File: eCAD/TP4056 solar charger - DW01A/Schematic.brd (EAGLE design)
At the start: 71.1 x 28.9 mm, 33 parts, among them IC1 TP4056X, IC2 AP9101CK6-ADTRG1, IC3 FDS6898A, Q1 SI2347DS-T1-GE3, X1 PV_PANEL, X2 BATTERY, X3 OUTPUT

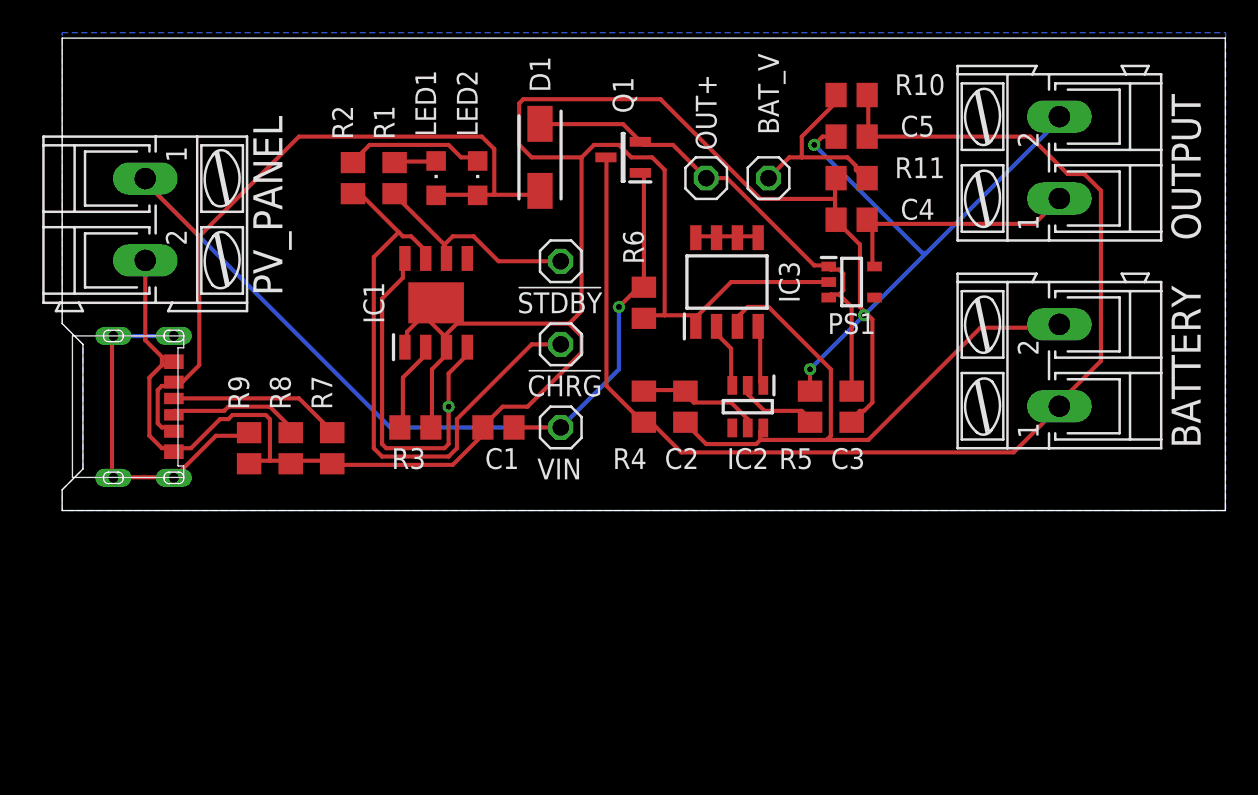
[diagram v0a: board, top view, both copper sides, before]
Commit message: RTC example and test
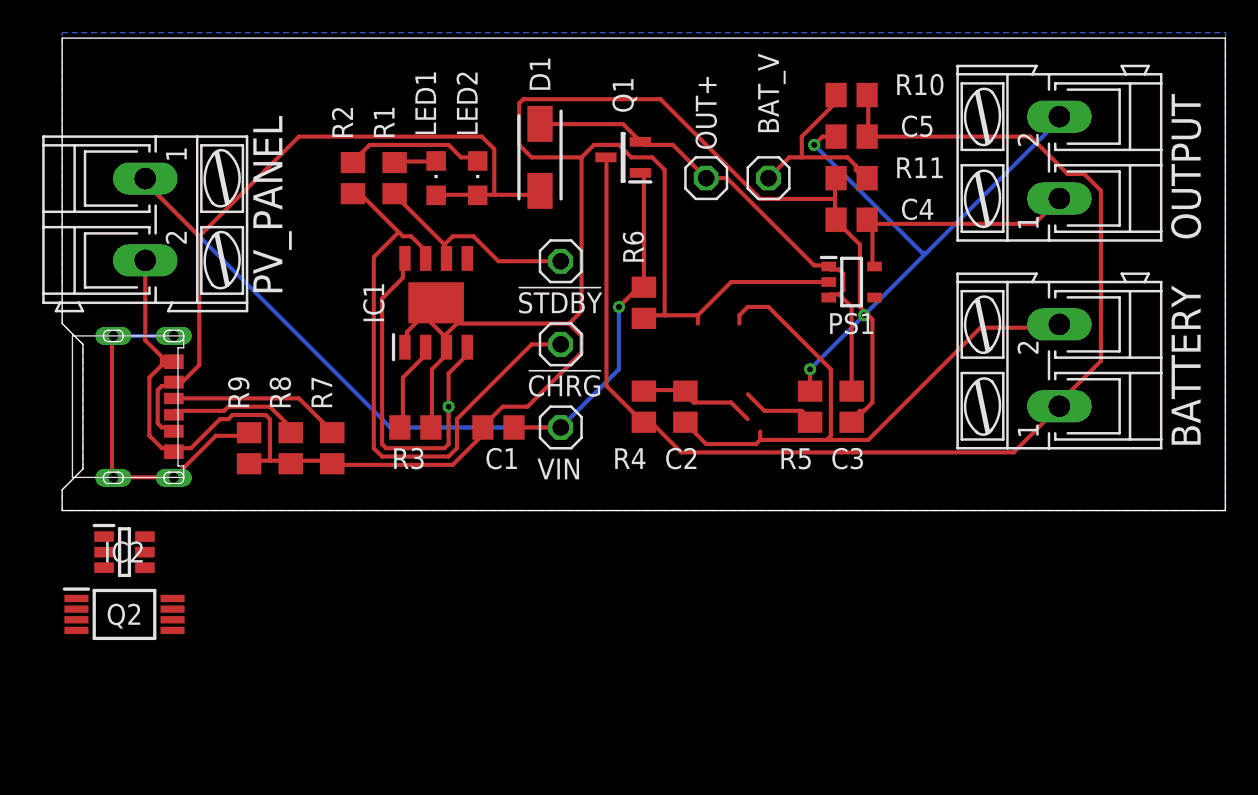
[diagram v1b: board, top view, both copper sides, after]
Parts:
- removed IC3: FDS6898A, 1-component-search:SOIC127P600X175-8N
- added Q2: FS8205A, 1-component-search:SOP65P640X120-8N
- IC2: value AP9101CK6-ADTRG1 -> DW01A-G; device 1-component-search:SOT95P285X140-6N -> 1-component-search:SOT95P280X135-6N
- moved IC2 39.1 mm to (3.81, -2.54), turned to 0 degrees
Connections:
- removed net N$10: IC2.1, IC3.4
- removed net N$12: IC2.3, IC3.2
- removed net N$13: IC3.5, IC3.6, IC3.7, IC3.8
- net BAT-: no longer IC2.6, IC3.3
- net GND: no longer IC3.1
- net N$5: no longer IC2.5
- net N$9: no longer IC2.2
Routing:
- net N$12: track 4.00 -> 0.00 mm
- net N$13: track 3.96 -> 0.00 mm
- net N$10: track 3.75 -> 0.00 mm
- net GND: track 188.8 -> 187.9 mm
- net N$9: track 5.17 -> 4.63 mm
- net N$5: track 7.84 -> 7.30 mm
- net BAT-: track 39.9 -> 39.4 mm

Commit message: DW01A schematic, removed eagle.epf from gitignore
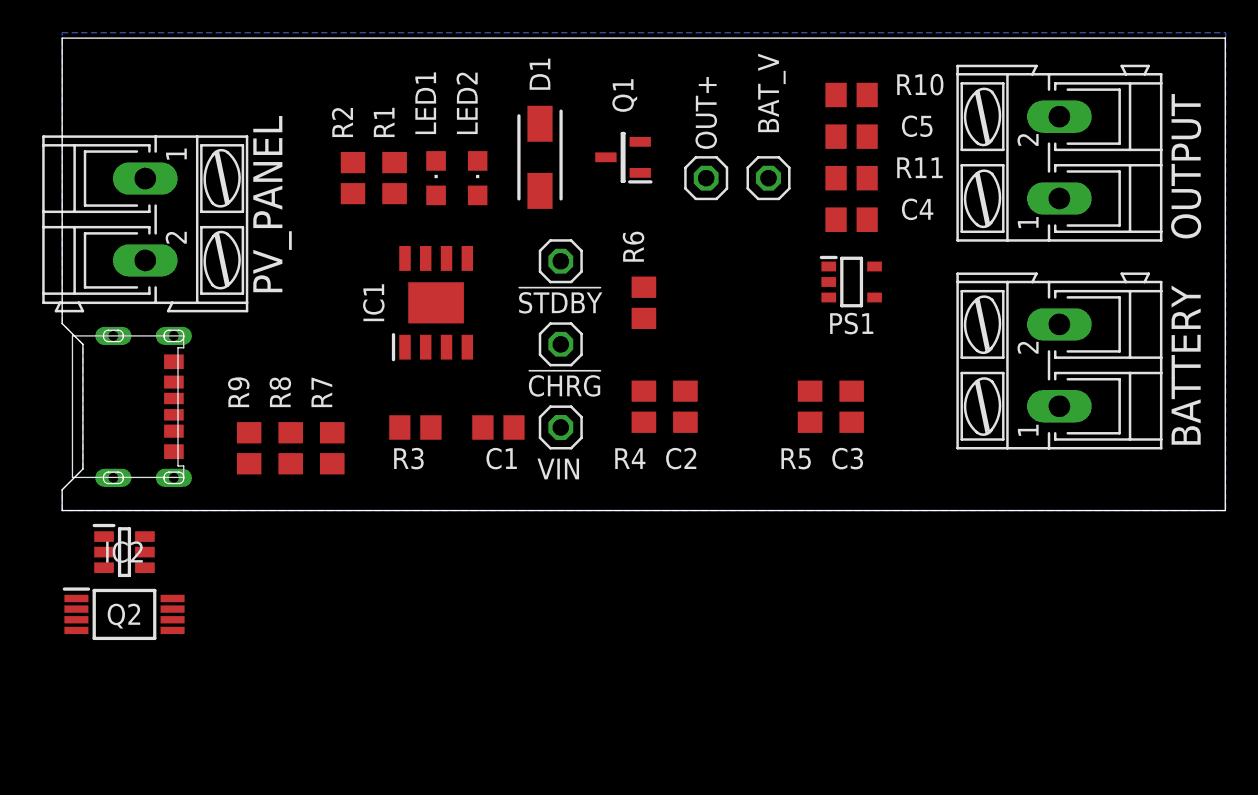
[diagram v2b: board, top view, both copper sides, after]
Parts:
- R4: value 330R -> 100R
- R5: value 2k7 -> 1k
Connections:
- new net N$10: IC2.1, Q2.4
- new net N$12: IC2.3, Q2.5
- net BAT-: now also Q2.2, Q2.3
- net GND: now also IC2.6, Q2.6, Q2.7
- net N$5: now also IC2.5
- net N$9: now also IC2.2
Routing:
- net GND: track 187.9 -> 0.00 mm, vias 3 -> 0
- net VIN: track 126.2 -> 0.00 mm, vias 2 -> 0
- net OUTPUT: track 77.1 -> 0.00 mm
- net BAT-: track 39.4 -> 0.00 mm
- net N$6: track 35.8 -> 0.00 mm
- net OUT+: track 30.7 -> 0.00 mm
- net N$7: track 22.1 -> 0.00 mm
- net N$14: track 15.6 -> 0.00 mm
- net N$3: track 13.2 -> 0.00 mm
- net N$15: track 11.9 -> 0.00 mm
- net N$11: track 10.6 -> 0.00 mm
- net N$2: track 8.64 -> 0.00 mm
- net N$8: track 8.31 -> 0.00 mm
- net N$5: track 7.30 -> 0.00 mm
- net N$4: track 5.69 -> 0.00 mm
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
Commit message: Created version of charger with JLC stock parts
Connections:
- net BAT-: now also IC2.6
- net GND: no longer IC2.6
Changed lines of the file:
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@@
 <contactref element="Q2" pad="6"/>
 <contactref element="Q2" pad="7"/>
-<contactref element="IC2" pad="6"/>
 <wire x1="47.31" y1="22.86" x2="60.96" y2="24.0792" width="0" layer="19" extent="1-1"/>
 <wire x1="47.31" y1="20.32" x2="47.31" y2="22.86" width="0" layer="19" extent="1-1"/>
@@
 <wire x1="6.83" y1="3.6" x2="11.43" y2="2.86" width="0" layer="19" extent="1-1"/>
 <wire x1="6.83" y1="9.1" x2="6.83" y2="3.6" width="0" layer="19" extent="1-1"/>
-<wire x1="5.06" y1="-1.59" x2="6.83" y2="3.6" width="0" layer="19" extent="1-1"/>
-<wire x1="6.748" y1="-6.025" x2="5.06" y2="-1.59" width="0" layer="19" extent="1-1"/>
+<wire x1="5.08" y1="15.2908" x2="6.83" y2="9.1" width="0" layer="19" extent="1-1"/>
+<wire x1="6.748" y1="-6.025" x2="6.83" y2="3.6" width="0" layer="19" extent="1-1"/>
 <wire x1="6.748" y1="-6.675" x2="6.748" y2="-6.025" width="0" layer="19" extent="1-1"/>
-<wire x1="5.08" y1="15.2908" x2="6.83" y2="9.1" width="0" layer="19" extent="1-1"/>
 </signal>
 <signal name="N$5">
@@
 <contactref element="Q2" pad="2"/>
 <contactref element="Q2" pad="3"/>
+<contactref element="IC2" pad="6"/>
 <wire x1="38.1" y1="5.4" x2="60.96" y2="11.3792" width="0" layer="19" extent="1-1"/>
-<wire x1="0.872" y1="-6.025" x2="38.1" y2="5.4" width="0" layer="19" extent="1-1"/>
+<wire x1="5.06" y1="-1.59" x2="38.1" y2="5.4" width="0" layer="19" extent="1-1"/>
+<wire x1="0.872" y1="-6.025" x2="5.06" y2="-1.59" width="0" layer="19" extent="1-1"/>
 <wire x1="0.872" y1="-6.675" x2="0.872" y2="-6.025" width="0" layer="19" extent="1-1"/>
 </signal>

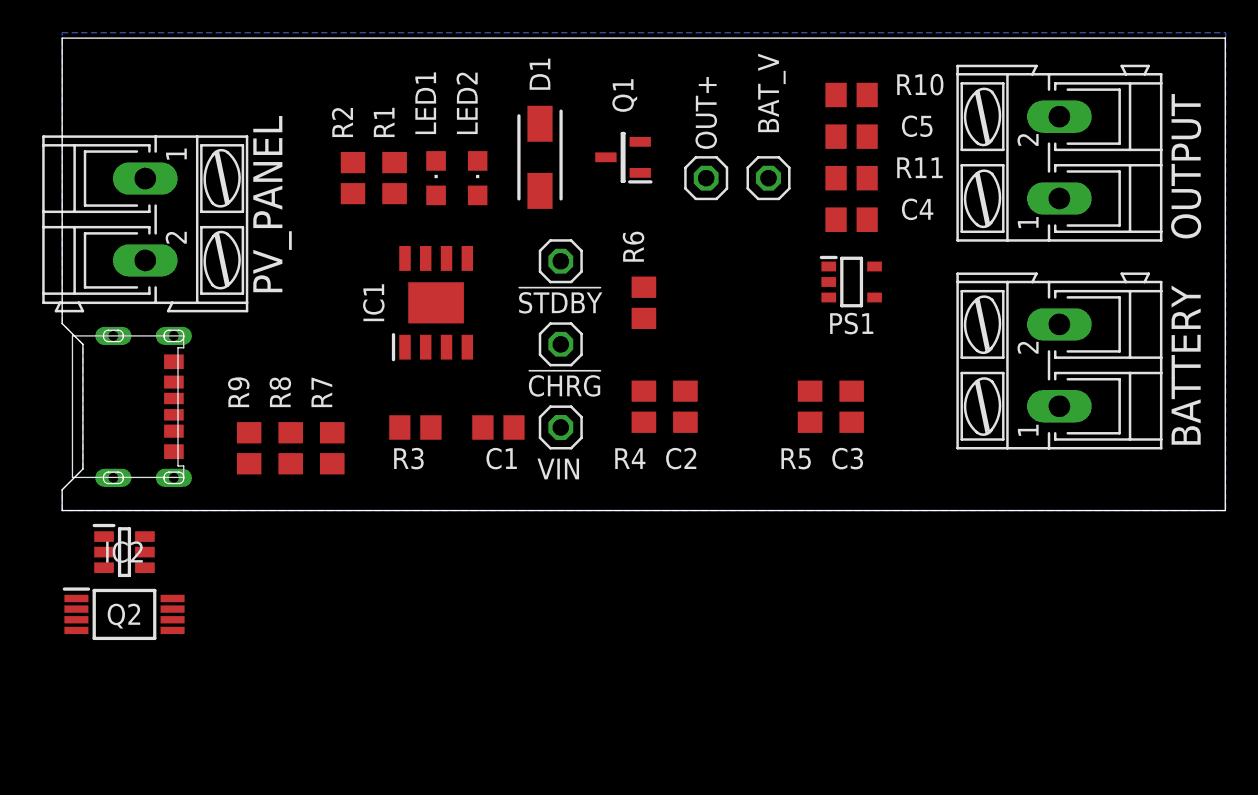
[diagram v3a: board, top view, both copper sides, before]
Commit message: Added power circuits, connection to Quectel devkit
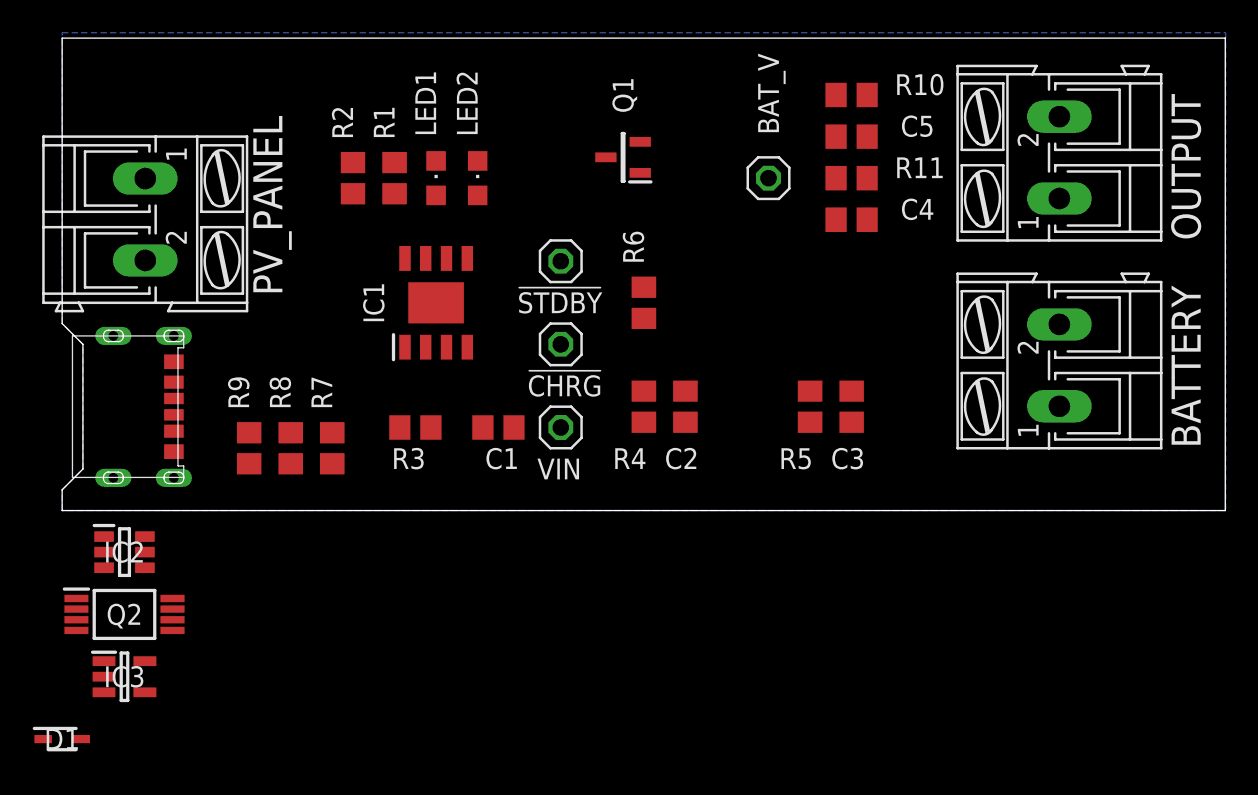
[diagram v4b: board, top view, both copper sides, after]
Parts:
- removed JP4: OUT+, pinhead:1X01
- removed PS1: BU33SD5WG-TR, 1-component-search:SOT95P280X125-5N
- added IC3: ME6211C33M5G-N, 1-component-search:SOT95P270X145-5N
- C3, C4: value 470n -> 1u
- D1: value STPS2L30A -> 1N4148WS-7-F; device 1-component-search:DIOM5126X265N -> 1-component-search:SOD2513X120N
- moved D1 46.0 mm to (0.00, -14.0), turned to 0 degrees
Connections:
- net GND: now also IC3.2; no longer PS1.2
- net N$14: now also IC3.5; no longer PS1.5
- net OUT+: now also IC3.1, IC3.3; no longer JP4.1, PS1.1, PS1.3
